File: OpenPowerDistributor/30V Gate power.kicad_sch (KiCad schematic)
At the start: 8 parts, among them U2 LGS6302

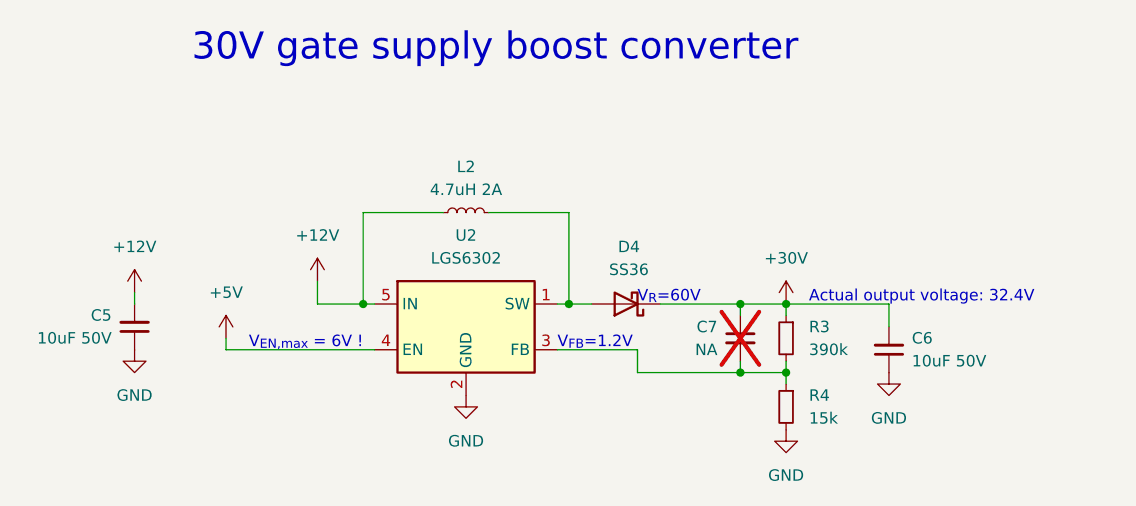
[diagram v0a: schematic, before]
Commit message: Added manual high side power switch
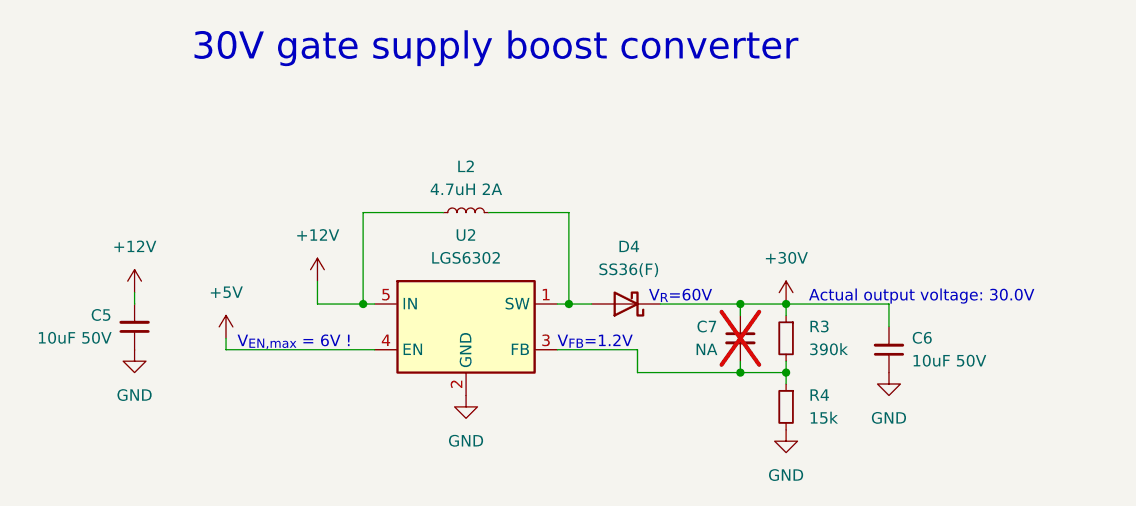
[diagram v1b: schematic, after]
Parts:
- D4: value SS36 -> SS36(F)
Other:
- note added: "Actual output voltage: 30.0V"
- note removed: "Actual output voltage: 32.4V"
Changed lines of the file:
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@@
     (stroke (width 0) (type default))
   )
-  (text "Actual output voltage: 32.4V" (at 171.45 85.09 0)
+  (text "Actual output voltage: 30.0V" (at 171.45 85.09 0)
     (effects (font (size 1.27 1.27)) (justify left bottom))
   )
-  (text "V_{EN,max} = 6V !" (at 109.22 90.17 0)
+  (text "V_{EN,max} = 6V !" (at 107.95 90.17 0)
     (effects (font (size 1.27 1.27)) (justify left bottom))
   )
@@
     (effects (font (size 3 3)) (justify left bottom))
   )
-  (text "V_{R}=60V" (at 152.4 85.09 0)
+  (text "V_{R}=60V" (at 153.67 85.09 0)
     (effects (font (size 1.27 1.27)) (justify left bottom))
   )
@@
       (effects (font (size 1.27 1.27)))
     )
-    (property "Value" "SS36" (at 151.4475 81.28 0)
-      (effects (font (size 1.27 1.27)))
-    )
+    (property "Value" "SS36(F)" (at 151.4475 81.28 0)
+      (effects (font (size 1.27 1.27)))
+    )

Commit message: More schematic progress
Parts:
- C7: footprint (none) -> Capacitor_SMD:C_0603_1608Metric
- R3, R4: footprint (none) -> Resistor_SMD:R_0603_1608Metric
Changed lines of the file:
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@@
       (effects (font (size 1.27 1.27)) (justify right))
     )
-    (property "Footprint" "" (at 163.83 88.9 0)
+    (property "Footprint" "Capacitor_SMD:C_0603_1608Metric" (at 163.83 88.9 0)
       (effects (font (size 1.27 1.27)) hide)
     )
@@
       (effects (font (size 1.27 1.27)) (justify right))
     )
-    (property "Footprint" "" (at 168.91 88.9 0)
+    (property "Footprint" "Resistor_SMD:R_0603_1608Metric" (at 168.91 88.9 0)
       (effects (font (size 1.27 1.27)) hide)
     )
@@
       (effects (font (size 1.27 1.27)) (justify right))
     )
-    (property "Footprint" "" (at 168.91 96.52 0)
-      (effects (font (size 1.27 1.27)) hide)
-    )
+    (property "Footprint" "Resistor_SMD:R_0603_1608Metric" (at 168.91 96.52 0)
+      (effects (font (size 1.27 1.27)) hide)
+    )

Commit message: Start to make layout
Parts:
- renumbered C7 to C10, C6 to C11, C5 to C9, L2 to L3, R3 to R5, R4 to R6, U2 to U3
